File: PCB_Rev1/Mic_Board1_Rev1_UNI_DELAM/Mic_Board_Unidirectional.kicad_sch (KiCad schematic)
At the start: 30 parts, among them J1 Conn_01x03_Pin, J2 532610771, J3 S2B-ZR-SM4A-TF_LF__SN_, U1 OPA1671IDBVR

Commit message: MICBOARD
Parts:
- removed J1: Conn_01x03_Pin, Connector_PinHeader_2.54mm:PinHeader_1x03_P2.54mm_Vertical, symbol Connector:Conn_01x03_Pin
- added R8, R9: 10k, Resistor_SMD:R_0805_2012Metric, symbol Device:R_Small_US
- R7: value 1k -> 18k
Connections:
- net +3V3: now also J2.6, R8.2; no longer J2.5
- net GND: now also J2.7, R9.1; no longer J2.6
- net at J2.1: now also U2.10 (LRCK); no longer U2.9 (SDTO)
- net at J2.2: now also U2.12 (BICK); no longer U2.10 (LRCK)
- net at U2.11 (MCLK): now also R9.2; no longer J2.3
- net at J2.4: no longer U2.12 (BICK)
- net at U2.13 (PDN): now also R8.1
- net at U2.15 (FSEL): now also J2.3
- no-connect marks 1 -> 4
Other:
- moved on the sheet: J2, R7

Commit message: New MIC Board UNI
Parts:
- added J1: 533980271, Footprints:SDTO_2_PIN_CONN, symbol 2 PIN:533980271
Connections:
- net at U2.9 (SDTO): now also J1.1
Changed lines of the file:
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@@
+	)
+	(no_connect
+		(at 228.6 111.76)
 	)
 	(no_connect
@@
 		(at 262.89 91.44)
 	)
-	(no_connect
-		(at 234.95 101.6)
-	)
 	(wire
 		(pts
@@
 	(wire
 		(pts
+			(xy 234.95 111.76) (xy 234.95 101.6)
+		)
+		(stroke
+			(width 0)
+			(type default)
+		)
+	)
+	(wire
+		(pts
 			(xy 151.13 114.3) (xy 151.13 116.84)
 		)
@@
 		(pts
 			(xy 243.84 106.68) (xy 247.65 106.68)
+		)
+		(stroke
+			(width 0)
+			(type default)
+		)
+	)
+	(wire
+		(pts
+			(xy 231.14 111.76) (xy 234.95 111.76)
 		)
 		(stroke
@@
 					(unit 1)
 				)
+			)
+		)
+	)
+	(symbol
+		(lib_id "2 PIN:533980271")
+		(at 231.14 111.76 270)
+		(unit 1)
+		(exclude_from_sim no)
+		(in_bom yes)
+		(on_board yes)
+		(dnp no)
+		(fields_autoplaced yes)
+		(property "Reference" "J1"
+			(at 234.95 119.3799 90)
+			(effects
+				(font
+					(size 1.524 1.524)
+				)
+				(justify left)
+			)
+		)
+		(property "Value" "533980271"
+			(at 234.95 121.9199 90)
+			(effects
+				(font
+					(size 1.524 1.524)
+				)
+				(justify left)
+			)
+		)
+		(property "Footprint" "Footprints:SDTO_2_PIN_CONN"
+			(at 231.14 111.76 0)
+			(effects
+				(font
+					(size 1.27 1.27)
+					(italic yes)
+				)
+				(hide yes)
+			)
+		)
+		(property "Datasheet" "533980271"
+			(at 231.14 111.76 0)
+			(effects
+				(font
+					(size 1.27 1.27)
+					(italic yes)
+				)
+				(hide yes)
+			)
+		)
+		(property "Description" ""
+			(at 231.14 111.76 0)
+			(effects
+				(font
+					(size 1.27 1.27)
+				)
+				(hide yes)
+			)
+		)
+		(pin "2"
+		)
+		(pin "1"
+		)
+		(instances
+			(project ""
+				(path "/1178ae07-c232-447f-a548-6d4f89d4abce"
+					(reference "J1")
+					(unit 1)
+				)

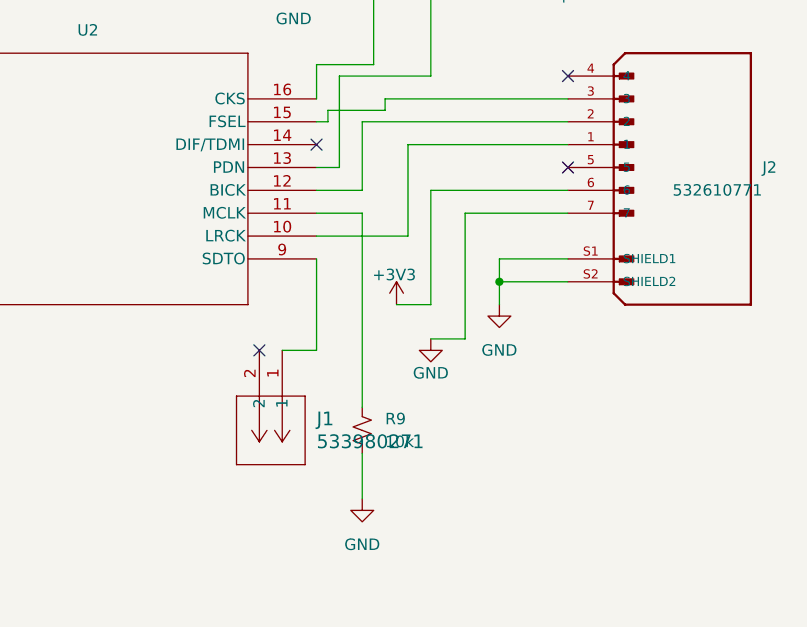
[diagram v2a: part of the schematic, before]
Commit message: Mic board updates
Removing connector and attaching to J instead
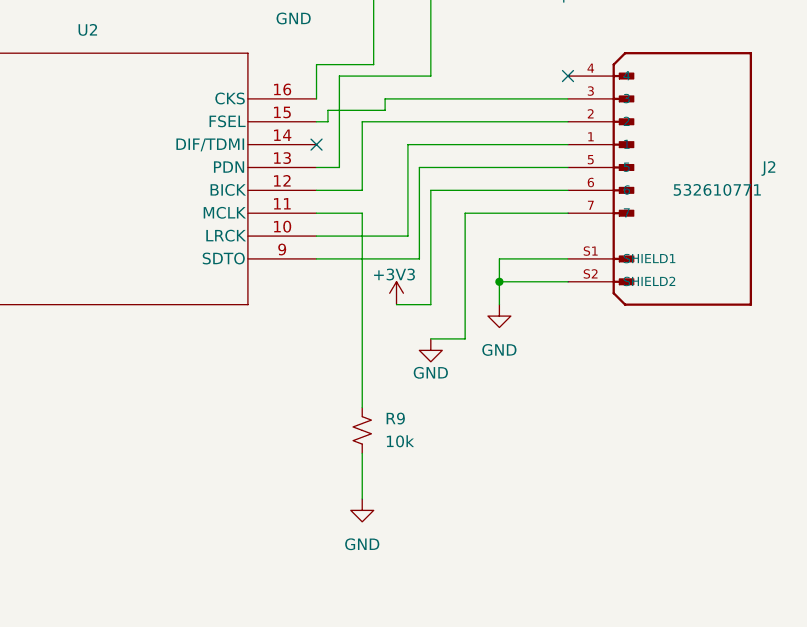
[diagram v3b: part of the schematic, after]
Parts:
- removed J1: 533980271, Footprints:SDTO_2_PIN_CONN, symbol 2 PIN:533980271
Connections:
- net at U2.9 (SDTO): now also J2.5
- no-connect marks 4 -> 2
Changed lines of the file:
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@@
-	)
-	(no_connect
-		(at 228.6 111.76)
 	)
 	(no_connect
@@
 		(at 262.89 81.28)
 	)
-	(no_connect
-		(at 262.89 91.44)
-	)
 	(wire
 		(pts
@@
 	(wire
 		(pts
-			(xy 234.95 111.76) (xy 234.95 101.6)
-		)
-		(stroke
-			(width 0)
-			(type default)
-		)
-	)
-	(wire
-		(pts
 			(xy 151.13 114.3) (xy 151.13 116.84)
 		)
@@
 	(wire
 		(pts
+			(xy 246.38 101.6) (xy 246.38 91.44)
+		)
+		(stroke
+			(width 0)
+			(type default)
+		)
+	)
+	(wire
+		(pts
 			(xy 241.3 69.85) (xy 237.49 69.85)
 		)
@@
 	(wire
 		(pts
+			(xy 234.95 101.6) (xy 246.38 101.6)
+		)
+		(stroke
+			(width 0)
+			(type default)
+		)
+	)
+	(wire
+		(pts
 			(xy 243.84 106.68) (xy 247.65 106.68)
 		)
@@
 	(wire
 		(pts
-			(xy 231.14 111.76) (xy 234.95 111.76)
-		)
-		(stroke
-			(width 0)
-			(type default)
-		)
-	)
-	(wire
-		(pts
 			(xy 240.03 123.19) (xy 240.03 128.27)
 		)
@@
 		(pts
 			(xy 247.65 81.28) (xy 247.65 71.12)
+		)
+		(stroke
+			(width 0)
+			(type default)
+		)
+	)
+	(wire
+		(pts
+			(xy 246.38 91.44) (xy 262.89 91.44)
 		)
 		(stroke
@@
 					(unit 1)
 				)
-			)
-		)
-	)
-	(symbol
-		(lib_id "2 PIN:533980271")
-		(at 231.14 111.76 270)
-		(unit 1)
-		(exclude_from_sim no)
-		(in_bom yes)
-		(on_board yes)
-		(dnp no)
-		(fields_autoplaced yes)
-		(property "Reference" "J1"
-			(at 234.95 119.3799 90)
-			(effects
-				(font
-					(size 1.524 1.524)
-				)
-				(justify left)
-			)
-		)
-		(property "Value" "533980271"
-			(at 234.95 121.9199 90)
-			(effects
-				(font
-					(size 1.524 1.524)
-				)
-				(justify left)
-			)
-		)
-		(property "Footprint" "Footprints:SDTO_2_PIN_CONN"
-			(at 231.14 111.76 0)
-			(effects
-				(font
-					(size 1.27 1.27)
-					(italic yes)
-				)
-				(hide yes)
-			)
-		)
-		(property "Datasheet" "533980271"
-			(at 231.14 111.76 0)
-			(effects
-				(font
-					(size 1.27 1.27)
-					(italic yes)
-				)
-				(hide yes)
-			)
-		)
-		(property "Description" ""
-			(at 231.14 111.76 0)
-			(effects
-				(font
-					(size 1.27 1.27)
-				)
-				(hide yes)
-			)
-		)
-		(pin "2"
-		)
-		(pin "1"
-		)
-		(instances
-			(project ""
-				(path "/1178ae07-c232-447f-a548-6d4f89d4abce"
-					(reference "J1")
-					(unit 1)
-				)

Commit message: New again
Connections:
- net at J2.1: now also U2.12 (BICK); no longer U2.10 (LRCK)
- net at J2.2: no longer U2.12 (BICK)
- net at J2.3: now also U2.10 (LRCK); no longer U2.15 (FSEL)
- net at J2.4: now also U2.9 (SDTO)
- net at J2.5: now also U2.15 (FSEL); no longer U2.9 (SDTO)
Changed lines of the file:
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@@
+	)
+	(no_connect
+		(at 262.89 86.36)
 	)
 	(no_connect
 		(at 234.95 88.9)
 	)
-	(no_connect
-		(at 262.89 81.28)
-	)
 	(wire
 		(pts
@@
 	(wire
 		(pts
-			(xy 234.95 93.98) (xy 240.03 93.98)
-		)
-		(stroke
-			(width 0)
-			(type default)
-		)
-	)
-	(wire
-		(pts
 			(xy 254 71.12) (xy 259.08 71.12)
 		)
@@
 	(wire
 		(pts
+			(xy 252.73 91.44) (xy 262.89 91.44)
+		)
+		(stroke
+			(width 0)
+			(type default)
+		)
+	)
+	(wire
+		(pts
 			(xy 151.13 114.3) (xy 151.13 116.84)
 		)
@@
 	(wire
 		(pts
+			(xy 241.3 99.06) (xy 234.95 99.06)
+		)
+		(stroke
+			(width 0)
+			(type default)
+		)
+	)
+	(wire
+		(pts
 			(xy 41.91 59.69) (xy 30.48 59.69)
 		)
@@
 	(wire
 		(pts
+			(xy 234.95 101.6) (xy 246.38 101.6)
+		)
+		(stroke
+			(width 0)
+			(type default)
+		)
+	)
+	(wire
+		(pts
+			(xy 262.89 83.82) (xy 241.3 83.82)
+		)
+		(stroke
+			(width 0)
+			(type default)
+		)
+	)
+	(wire
+		(pts
 			(xy 251.46 96.52) (xy 262.89 96.52)
 		)
@@
 	(wire
 		(pts
-			(xy 246.38 101.6) (xy 246.38 91.44)
-		)
-		(stroke
-			(width 0)
-			(type default)
-		)
-	)
-	(wire
-		(pts
 			(xy 241.3 69.85) (xy 237.49 69.85)
 		)
@@
 	(wire
 		(pts
+			(xy 238.76 88.9) (xy 238.76 93.98)
+		)
+		(stroke
+			(width 0)
+			(type default)
+		)
+	)
+	(wire
+		(pts
 			(xy 101.6 86.36) (xy 97.79 86.36)
 		)
@@
 	(wire
 		(pts
-			(xy 234.95 99.06) (xy 245.11 99.06)
-		)
-		(stroke
-			(width 0)
-			(type default)
-		)
-	)
-	(wire
-		(pts
 			(xy 81.28 92.71) (xy 81.28 95.25)
 		)
@@
 	(wire
 		(pts
-			(xy 236.22 86.36) (xy 234.95 86.36)
+			(xy 246.38 101.6) (xy 246.38 82.55)
 		)
 		(stroke
@@
 	(wire
 		(pts
-			(xy 234.95 101.6) (xy 246.38 101.6)
-		)
-		(stroke
-			(width 0)
-			(type default)
-		)
-	)
-	(wire
-		(pts
 			(xy 243.84 106.68) (xy 247.65 106.68)
 		)
@@
 	(wire
 		(pts
-			(xy 240.03 86.36) (xy 262.89 86.36)
-		)
-		(stroke
-			(width 0)
-			(type default)
-		)
-	)
-	(wire
-		(pts
 			(xy 180.34 88.9) (xy 180.34 86.36)
 		)
@@
 	(wire
 		(pts
+			(xy 238.76 93.98) (xy 234.95 93.98)
+		)
+		(stroke
+			(width 0)
+			(type default)
+		)
+	)
+	(wire
+		(pts
 			(xy 241.3 80.01) (xy 241.3 69.85)
 		)
@@
 	(wire
 		(pts
+			(xy 241.3 83.82) (xy 241.3 99.06)
+		)
+		(stroke
+			(width 0)
+			(type default)
+		)
+	)
+	(wire
+		(pts
 			(xy 40.64 93.98) (xy 44.45 93.98)
 		)
@@
 	(wire
 		(pts
-			(xy 246.38 91.44) (xy 262.89 91.44)
-		)
-		(stroke
-			(width 0)
-			(type default)
-		)
-	)
-	(wire
-		(pts
 			(xy 142.24 88.9) (xy 144.78 88.9)
 		)
@@
 	(wire
 		(pts
-			(xy 242.57 85.09) (xy 236.22 85.09)
+			(xy 234.95 86.36) (xy 252.73 86.36)
 		)
 		(stroke
@@
 	(wire
 		(pts
-			(xy 240.03 93.98) (xy 240.03 86.36)
-		)
-		(stroke
-			(width 0)
-			(type default)
-		)
-	)
-	(wire
-		(pts
-			(xy 262.89 83.82) (xy 242.57 83.82)
-		)
-		(stroke
-			(width 0)
-			(type default)
-		)
-	)
-	(wire
-		(pts
 			(xy 67.31 59.69) (xy 86.36 59.69)
 		)
@@
 	(wire
 		(pts
-			(xy 242.57 83.82) (xy 242.57 85.09)
-		)
-		(stroke
-			(width 0)
-			(type default)
-		)
-	)
-	(wire
-		(pts
 			(xy 97.79 86.36) (xy 97.79 109.22)
 		)
@@
 	(wire
 		(pts
-			(xy 245.11 88.9) (xy 262.89 88.9)
-		)
-		(stroke
-			(width 0)
-			(type default)
-		)
-	)
-	(wire
-		(pts
 			(xy 180.34 86.36) (xy 184.15 86.36)
 		)
@@
 	(wire
 		(pts
+			(xy 246.38 82.55) (xy 251.46 82.55)
+		)
+		(stroke
+			(width 0)
+			(type default)
+		)
+	)
+	(wire
+		(pts
+			(xy 251.46 82.55) (xy 251.46 81.28)
+		)
+		(stroke
+			(width 0)
+			(type default)
+		)
+	)
+	(wire
+		(pts
 			(xy 152.4 91.44) (xy 160.02 91.44)
 		)
@@
 	(wire
 		(pts
-			(xy 245.11 88.9) (xy 245.11 99.06)
+			(xy 252.73 86.36) (xy 252.73 91.44)
 		)
 		(stroke
@@
 	(wire
 		(pts
+			(xy 262.89 88.9) (xy 238.76 88.9)
+		)
+		(stroke
+			(width 0)
+			(type default)
+		)
+	)
+	(wire
+		(pts
 			(xy 237.49 91.44) (xy 237.49 81.28)
 		)
@@
 	(wire
 		(pts
-			(xy 236.22 85.09) (xy 236.22 86.36)
-		)
-		(stroke
+			(xy 251.46 81.28) (xy 262.89 81.28)
+		)
+		(stroke

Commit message: SAVE
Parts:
- C1, C10, C8, C9: LCSC (none) -> C519973
- C11: LCSC (none) -> C519977
- C2, C5, C6, C7: LCSC (none) -> C88484
- C3: LCSC (none) -> C576434
- C4: LCSC (none) -> C3857194
- J2: LCSC (none) -> C505276
- J3: LCSC (none) -> C265329
- R1: LCSC (none) -> C865529
- R2, R8, R9: LCSC (none) -> C110775
- R3, R4: LCSC (none) -> C96346
- R5: LCSC (none) -> C95781
- R6: LCSC (none) -> C868262
- R7: LCSC (none) -> C137468
- U1: LCSC (none) -> C1849409
- U2: LCSC (none) -> C1519002
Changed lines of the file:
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@@
 			)
 		)
+		(property "LCSC" "C1849409"
+			(at 142.24 88.9 0)
+			(effects
+				(font
+					(size 1.27 1.27)
+				)
+				(hide yes)
+			)
+		)
 		(pin "1"
 		)
@@
 			)
 		)
+		(property "LCSC" "C110775"
+			(at 240.03 120.65 0)
+			(effects
+				(font
+					(size 1.27 1.27)
+				)
+				(hide yes)
+			)
+		)
 		(pin "1"
 		)
@@
 			)
 		)
-		(property "Description" "\nPicoblade Connector, 7 Circuit Single Row, Right Angle Surface Mount SMT PCB\n"
+		(property "Description" "Picoblade Connector, 7 Circuit Single Row, Right Angle Surface Mount SMT PCB"
 			(at 275.59 91.44 0)
 			(effects
@@
 			)
 		)
+		(property "LCSC" "C505276"
+			(at 275.59 91.44 0)
+			(effects
+				(font
+					(size 1.27 1.27)
+				)
+				(hide yes)
+			)
+		)
 		(pin "4"
 		)
@@
 			)
 		)
+		(property "LCSC" "C96346"
+			(at 81.28 90.17 0)
+			(effects
+				(font
+					(size 1.27 1.27)
+				)
+				(hide yes)
+			)
+		)
 		(pin "1"
 		)
@@
 			)
 		)
+		(property "LCSC" "C96346"
+			(at 86.36 68.58 0)
+			(effects
+				(font
+					(size 1.27 1.27)
+				)
+				(hide yes)
+			)
+		)
 		(pin "1"
 		)
@@
 			)
 		)
+		(property "LCSC" "C519973"
+			(at 53.34 66.04 0)
+			(effects
+				(font
+					(size 1.27 1.27)
+				)
+				(hide yes)
+			)
+		)
 		(pin "1"
 		)
@@
 			)
 		)
+		(property "LCSC" "C865529"
+			(at 44.45 59.69 90)
+			(effects
+				(font
+					(size 1.27 1.27)
+				)
+				(hide yes)
+			)
+		)
 		(pin "1"
 		)
@@
 			)
 		)
+		(property "LCSC" "C110775"
+			(at 67.31 68.58 0)
+			(effects
+				(font
+					(size 1.27 1.27)
+				)
+				(hide yes)
+			)
+		)
 		(pin "1"
 		)
@@
 			)
 		)
+		(property "LCSC" "C519977"
+			(at 180.34 74.93 90)
+			(effects
+				(font
+					(size 1.27 1.27)
+				)
+				(hide yes)
+			)
+		)
 		(pin "1"
 		)
@@
 			)
 		)
+		(property "LCSC" "C265329"
+			(at 30.48 88.9 0)
+			(effects
+				(font
+					(size 1.27 1.27)
+				)
+				(hide yes)
+			)
+		)
 		(pin "2"
 		)
@@
 			)
 		)
+		(property "LCSC" "C1519002"
+			(at 184.15 83.82 0)
+			(effects
+				(font
+					(size 1.27 1.27)
+				)
+				(hide yes)
+			)
+		)
 		(pin "1"
 		)
@@
 			)
 		)
+		(property "LCSC" "C3857194"
+			(at 121.92 121.92 90)
+			(effects
+				(font
+					(size 1.27 1.27)
+				)
+				(hide yes)
+			)
+		)
 		(pin "1"
 		)
@@
 			)
 		)
+		(property "LCSC" "C88484"
+			(at 165.1 86.36 90)
+			(effects
+				(font
+					(size 1.27 1.27)
+				)
+				(hide yes)
+			)
+		)
 		(pin "1"
 		)
@@
 			)
 		)
+		(property "LCSC" "C88484"
+			(at 73.66 83.82 90)
+			(effects
+				(font
+					(size 1.27 1.27)
+				)
+				(hide yes)
+			)
+		)
 		(pin "1"
 		)
@@
 			)
 		)
+		(property "LCSC" "C137468"
+			(at 234.95 69.85 90)
+			(effects
+				(font
+					(size 1.27 1.27)
+				)
+				(hide yes)
+			)
+		)
 		(pin "1"
 		)
@@
 			)
 		)
+		(property "LCSC" "C868262"
+			(at 121.92 109.22 90)
+			(effects
+				(font
+					(size 1.27 1.27)
+				)
+				(hide yes)
+			)
+		)
 		(pin "1"
 		)
@@
 			)
 		)
+		(property "LCSC" "C95781"
+			(at 88.9 121.92 90)
+			(effects
+				(font
+					(size 1.27 1.27)
+				)
+				(hide yes)
+			)
+		)
 		(pin "1"
 		)
@@
 			)
 		)
+		(property "LCSC" "C519973"
+			(at 170.18 95.25 0)
+			(effects
+				(font
+					(size 1.27 1.27)
+				)
+				(hide yes)
+			)
+		)
 		(pin "1"
 		)
@@
 			)
 		)
+		(property "LCSC" "C576434"
+			(at 73.66 121.92 90)
+			(effects
+				(font
+					(size 1.27 1.27)
+				)
+				(hide yes)
+			)
+		)
 		(pin "1"
 		)
@@
 			)
 		)
+		(property "LCSC" "C88484"
+			(at 160.02 95.25 0)
+			(effects
+				(font
+					(size 1.27 1.27)
+				)
+				(hide yes)
+			)
+		)
 		(pin "1"
 		)
@@
 			)
 		)
+		(property "LCSC" "C110775"
+			(at 251.46 71.12 90)
+			(effects
+				(font
+					(size 1.27 1.27)
+				)
+				(hide yes)
+			)
+		)
 		(pin "1"
 		)
@@
 			)
 		)
+		(property "LCSC" "C88484"
+			(at 160.02 113.03 0)
+			(effects
+				(font
+					(size 1.27 1.27)
+				)
+				(hide yes)
+			)
+		)
 		(pin "1"
 		)
@@
 			)
 		)
+		(property "LCSC" "C519973"
+			(at 170.18 113.03 0)
+			(effects
+				(font
+					(size 1.27 1.27)
+				)
+				(hide yes)
+			)
+		)
 		(pin "1"
 		)
@@
 			(at 179.07 113.03 0)
 			(effects
+				(font
+					(size 1.27 1.27)
+				)
+				(hide yes)
+			)
+		)
+		(property "LCSC" "C519973"
+			(at 179.07 113.03 0)
+			(effects
